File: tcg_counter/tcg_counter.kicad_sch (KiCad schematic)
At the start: 0 parts

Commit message: Added dispay symbol to schematic and update TCAL9539
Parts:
- added U1: TCAL9539RTW, Package_DFN_QFN:Texas_RTW_WQFN-24-1EP_4x4mm_P0.5mm_EP2.7x2.7mm_ThermalVias, symbol Library:TCAL9539RTW
- added U2: ~, symbol Library:D0430G02V01
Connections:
- new net: U1.8 (P07), U2.1 (COM)
- new net: U1.14 (P14), U2.10 (2E)
- new net: U1.13 (P13), U2.11 (2D)
- new net: U1.12 (P12), U2.12 (2C)
- new net: U1.16 (P16), U2.13 (2G)
- new net: U1.11 (P11), U2.14 (2B)
- new net: U1.10 (P10), U2.15 (2A)
- new net: U1.15 (P15), U2.16 (2F)
- new net: U1.2 (P01), U2.2 (1B)
- new net: U1.1 (P00), U2.3 (1A)
- new net: U1.6 (P05), U2.4 (1F)
- new net: U1.17 (P17), U2.5 (3)
- new net: U1.7 (P06), U2.6 (1G)
- new net: U1.5 (P04), U2.7 (1E)
- new net: U1.4 (P03), U2.8 (1D)
- new net: U1.3 (P02), U2.9 (1C)
- new net GND: U1.18 (A0), U1.23 (A1), U1.9 (GND)

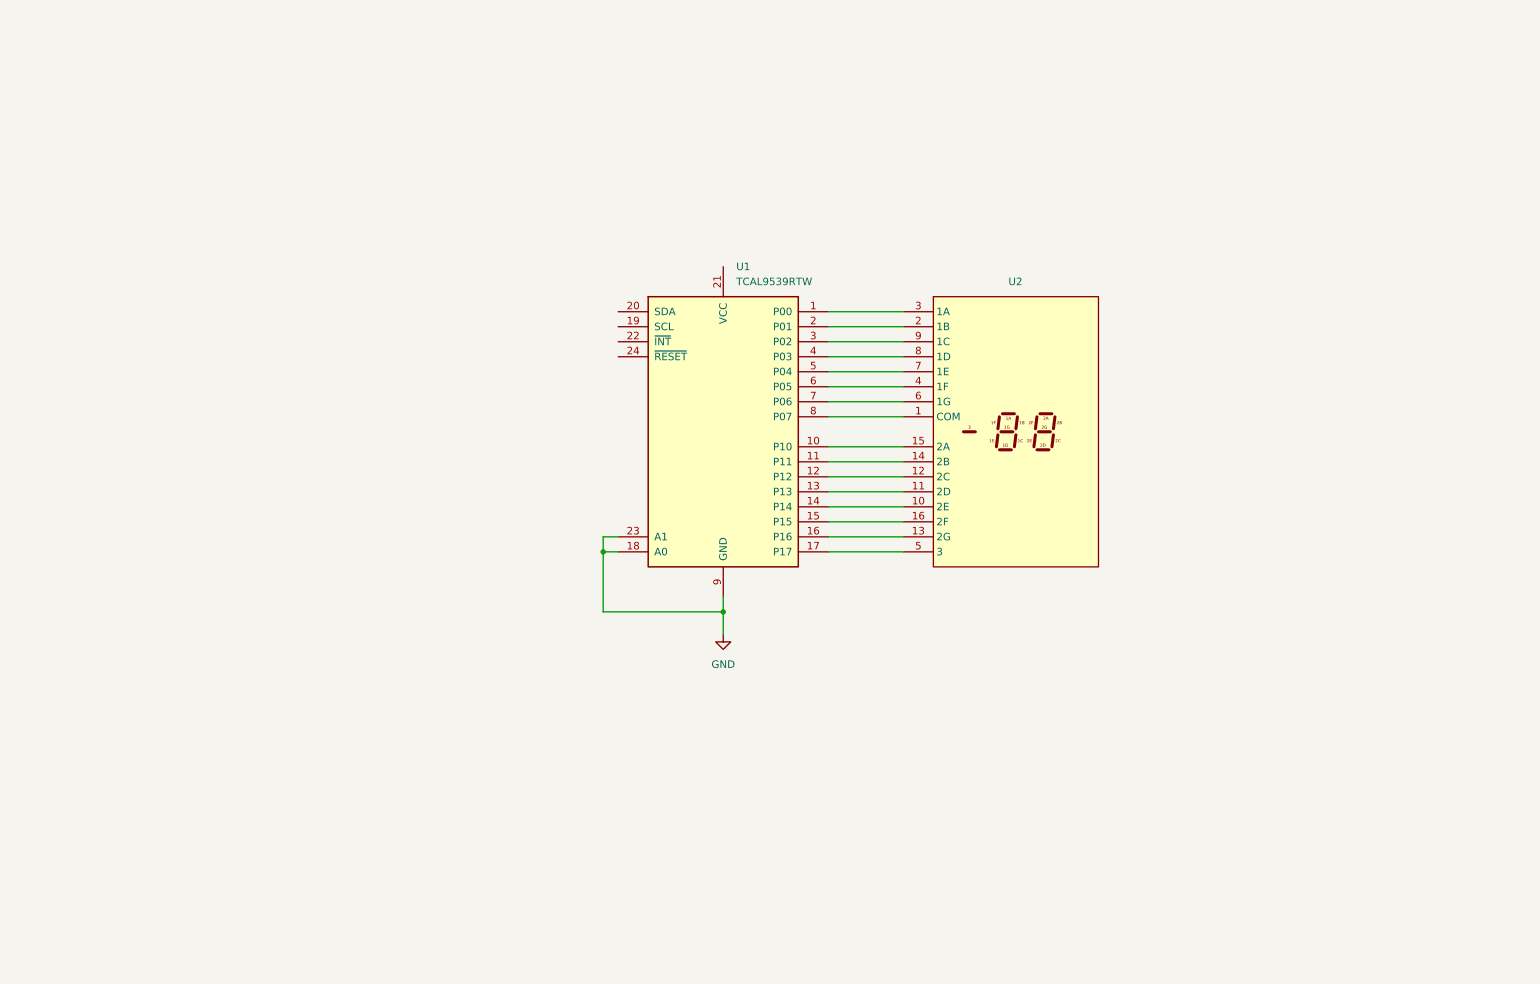
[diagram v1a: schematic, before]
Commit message: Added antenna trace from goodtag
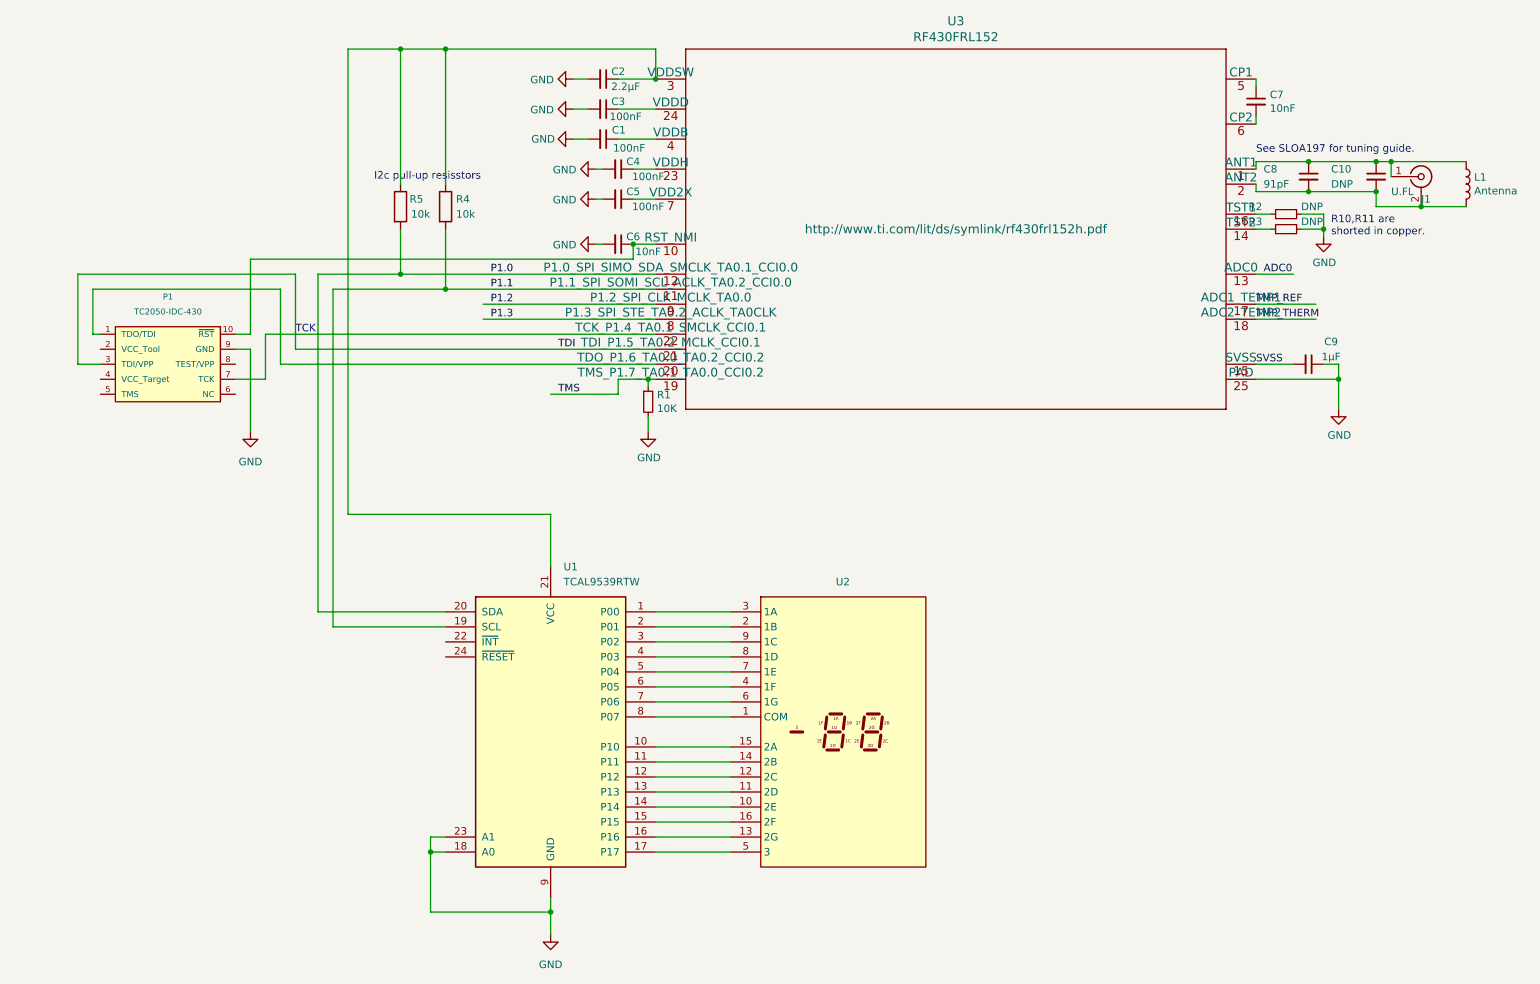
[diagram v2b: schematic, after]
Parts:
- added C1, C3, C4, C5: 100nF, Capacitor_SMD:C_0402_1005Metric, symbol Device:C_Small
- added C10: DNP, Capacitor_SMD:C_0402_1005Metric, symbol Device:C_Small
- added C2: 2.2µF, Capacitor_SMD:C_0402_1005Metric, symbol Device:C_Small
- added C6, C7: 10nF, Capacitor_SMD:C_0402_1005Metric, symbol Device:C_Small
- added C8: 91pF, Capacitor_SMD:C_0402_1005Metric, symbol Device:C_Small
- added C9: 1µF, Capacitor_SMD:C_0402_1005Metric, symbol Device:C_Small
- added J1: U.FL, Connector_Coaxial:U.FL_Molex_MCRF_73412-0110_Vertical, symbol Connector:Conn_Coaxial
- added L1: Antenna, footprints:GW10ANT, symbol Device:L
- added P1: TC2050-IDC-430, symbol Tag-Connect:TC2050-IDC-430
- added R1: 10K, Resistor_SMD:R_0402_1005Metric, symbol Device:R_Small
- added R2, R3: DNP, footprints:R_0402_shorted, symbol Device:R_Small
- added R4, R5: 10k, symbol Device:R
- added U3: RF430FRL152, footprints:RF430FRL152H, symbol symbols:RF430FRL152HRGE
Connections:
- net GND: now also C1.2, C2.2, C3.2, C4.2, C5.2, C6.2, C9.1, P1.9 (GND), R1.2, R2.1, R3.1, U3.25 (PAD)
- net P1.1: now reaches U1.19 (SCL)
- net P1.1: now also R4.2, U3.11 (P1.1_SPI_SOMI_SCL_ACLK_TA0.2_CCI0.0)
- net P1.0: now reaches U1.20 (SDA)
- net P1.0: now also R5.2, U3.12 (P1.0_SPI_SIMO_SDA_SMCLK_TA0.1_CCI0.0)
- net at U1.21 (VCC): now also C2.1, R4.1, R5.1, U3.3 (VDDSW)
- new net: R2.2, U3.16 (TST1)
- new net: R3.2, U3.14 (TST2)
- new net: C5.1, U3.7 (VDD2X)
- new net: C10.1, C8.1, J1.1 (In), L1.1, U3.1 (ANT1)
- new net: C10.2, C8.2, J1.2 (Ext), L1.2, U3.2 (ANT2)
- new net: C6.1, P1.10 (~{RST}), U3.10 (RST_NMI)
- new net: P1.1 (TDO/TDI), U3.20 (TDO_P1.6_TA0.0_TA0.2_CCI0.2)
- new net: C4.1, U3.23 (VDDH)
- new net: C3.1, U3.24 (VDDD)
- new net: C1.1, U3.4 (VDDB)
- new net: C7.1, U3.5 (CP1)
- new net: C7.2, U3.6 (CP2)
- new net ADC0: U3.13 (ADC0)
- new net P1.2: U3.9 (P1.2_SPI_CLK_MCLK_TA0.0)
- new net P1.3: U3.8 (P1.3_SPI_STE_TA0.2_ACLK_TA0CLK)
- new net SVSS: C9.2, U3.15 (SVSS)
- new net TCK: P1.3 (TDI/VPP), P1.7 (TCK), U3.21 (TDI_P1.5_TA0.2_MCLK_CCI0.1), U3.22 (TCK_P1.4_TA0.1_SMCLK_CCI0.1)
- new net TMP_REF: U3.17 (ADC1_TEMP1)
- new net TMP_THERM: U3.18 (ADC2_TEMP2)
- new net TMS: R1.1, U3.19 (TMS_P1.7_TA0.1_TA0.0_CCI0.2)
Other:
- note added: "I2c pull-up resisstors"
- note added: "R10,R11 are shorted in copper."
- note added: "See SLOA197 for tuning guide."
- moved on the sheet: U1, U2

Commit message: Added current limiting resistor
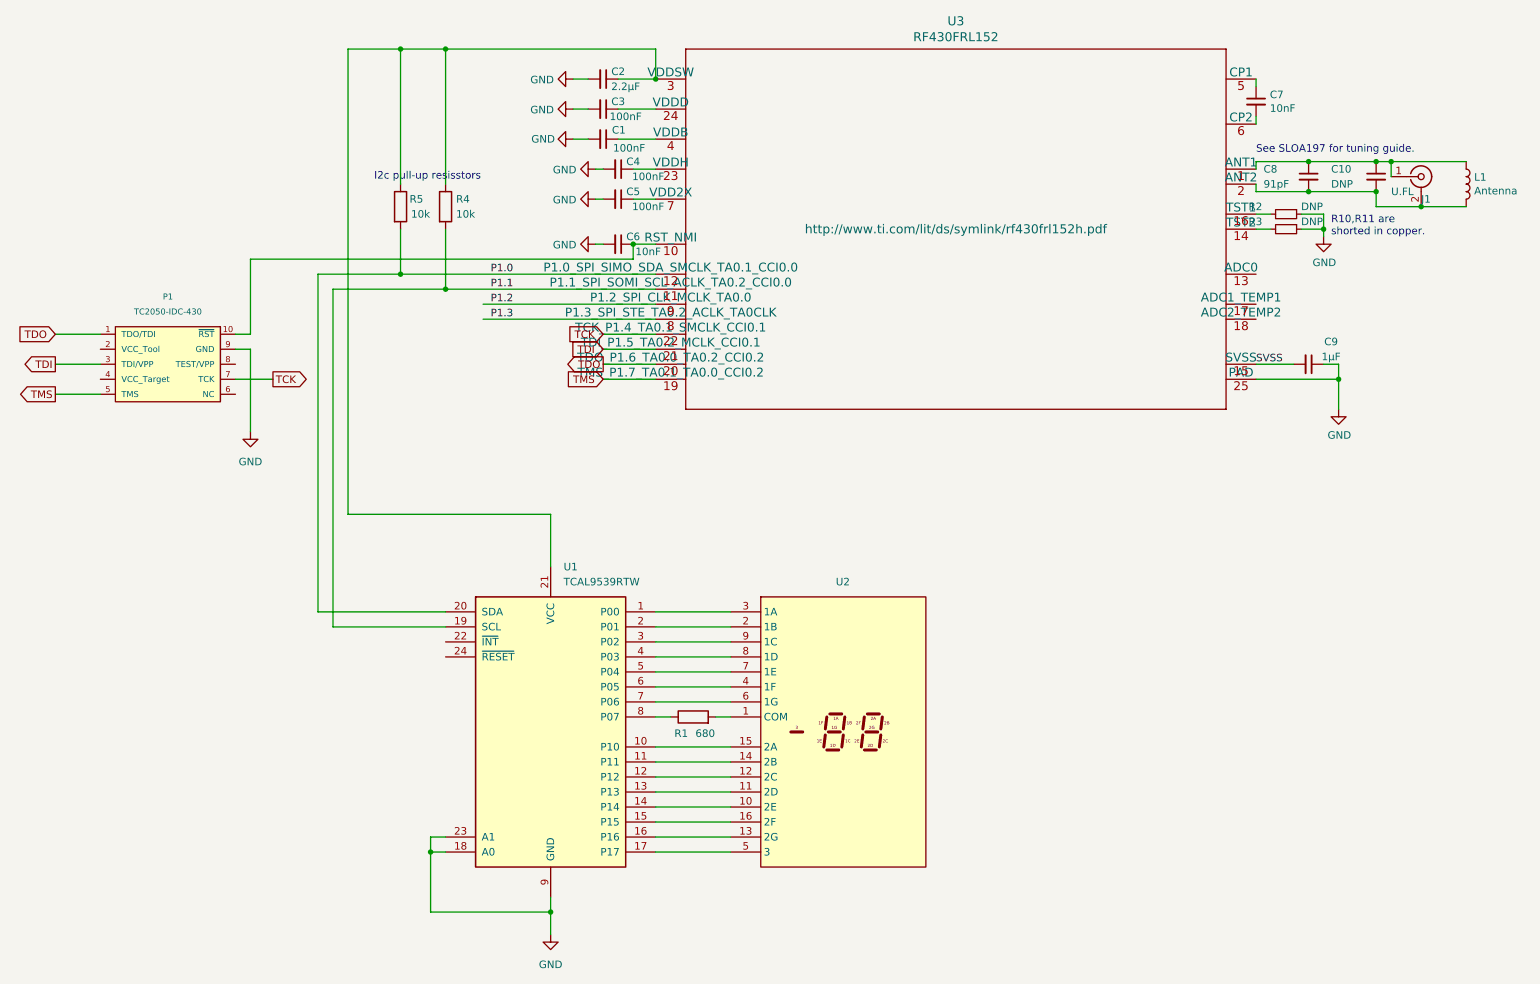
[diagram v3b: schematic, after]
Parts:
- removed R1: 10K, Resistor_SMD:R_0402_1005Metric, symbol Device:R_Small
- added R1: 680, symbol Device:R
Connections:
- net TCK: no longer P1.3 (TDI/VPP), U3.21 (TDI_P1.5_TA0.2_MCLK_CCI0.1)
- net TMS: now also P1.5 (TMS)
- net at U1.8 (P07): now also R1.1; no longer U2.1 (COM)
- net TDO: now reaches P1.1 (TDO/TDI), U3.20 (TDO_P1.6_TA0.0_TA0.2_CCI0.2)
- net ADC0: no longer names the net of U3.13 (ADC0)
- net TMP_REF: no longer names the net of U3.17 (ADC1_TEMP1)
- net TMP_THERM: no longer names the net of U3.18 (ADC2_TEMP2)
- new net: R1.2, U2.1 (COM)
- new net TDI: P1.3 (TDI/VPP), U3.21 (TDI_P1.5_TA0.2_MCLK_CCI0.1)
